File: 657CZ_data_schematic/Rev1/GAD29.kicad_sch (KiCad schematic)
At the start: 2 parts, among them J291 DE9_Socket, J292 DB25_Socket

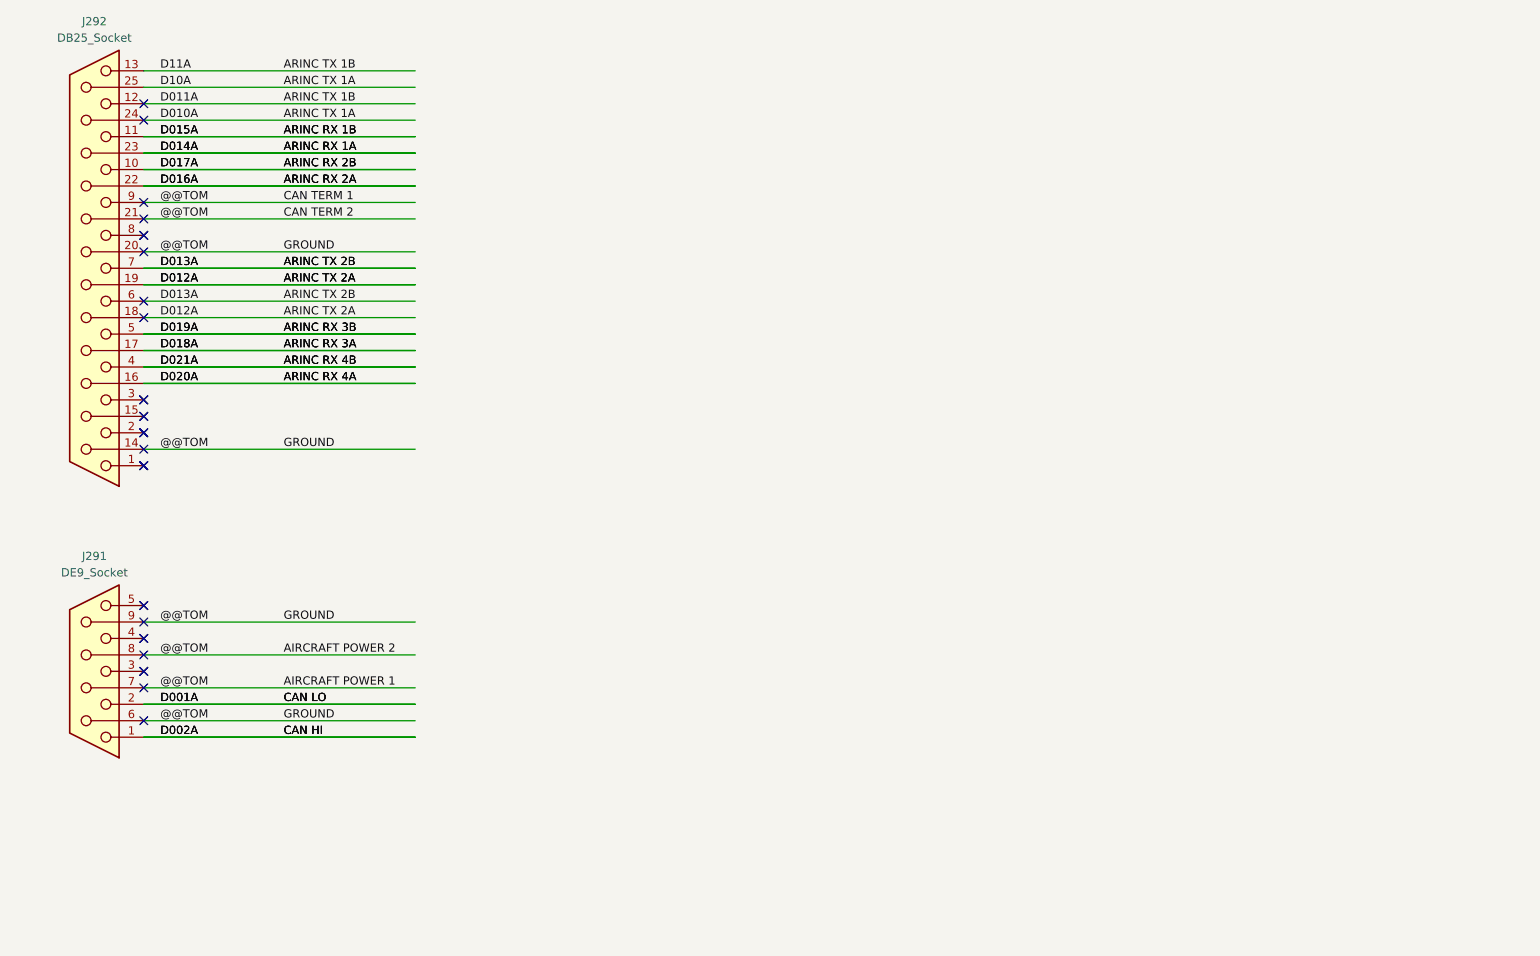
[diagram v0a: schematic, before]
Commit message: added data connections after AvClassics wiring. completed LRUs GMU, GDU, GSU, GAD, GNC, GTX, GTR  Not completed GMA, GEA and autopilot LRUs
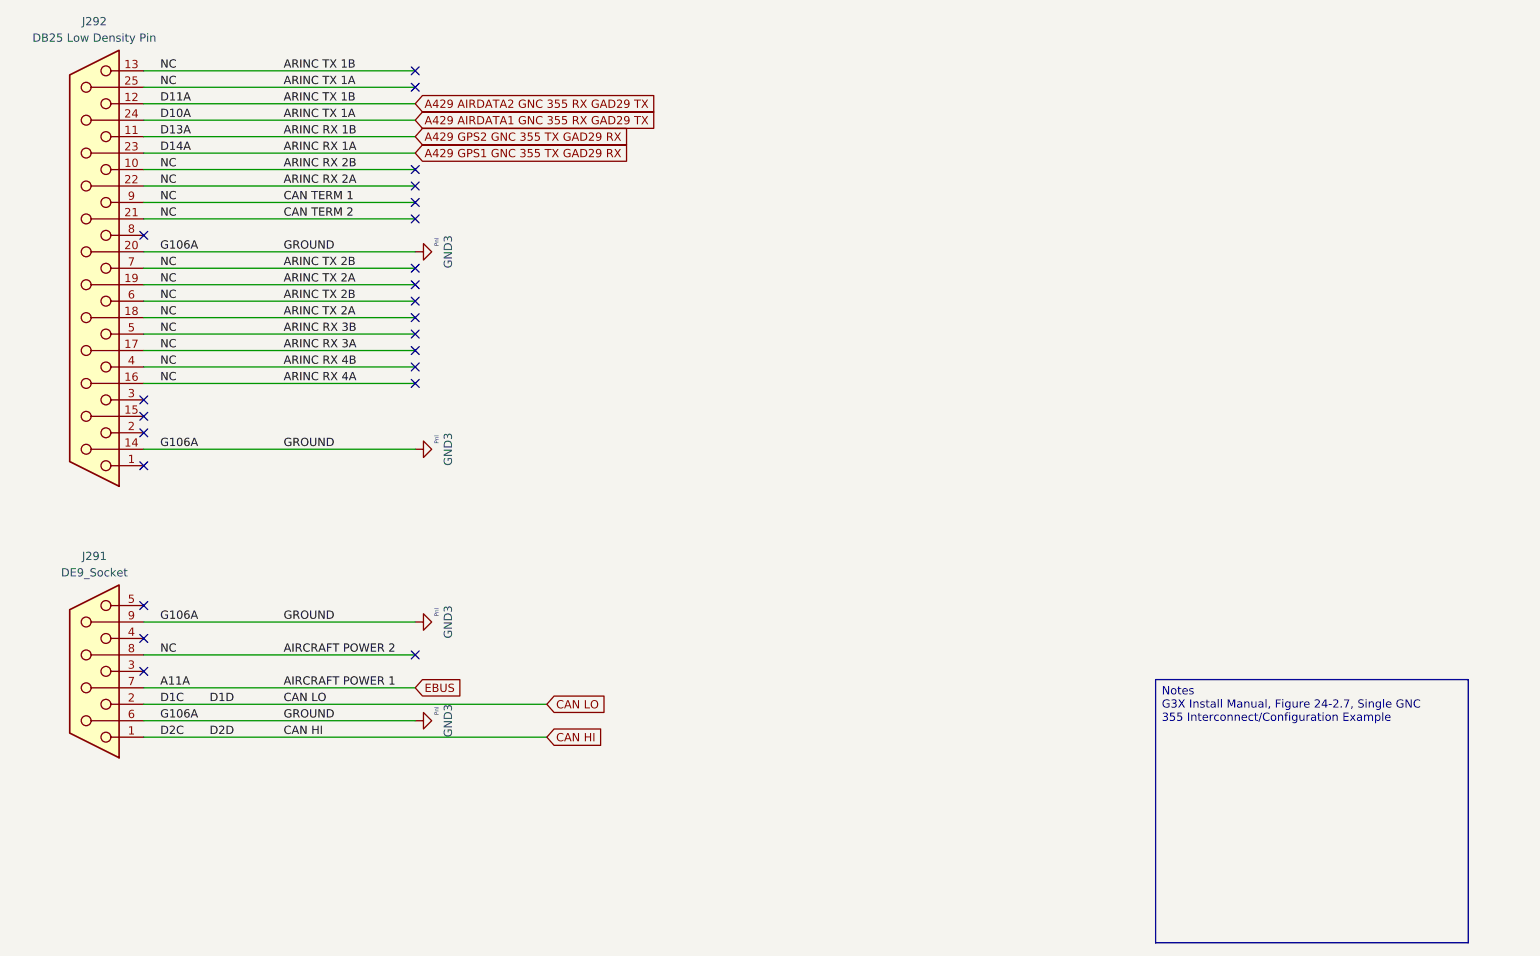
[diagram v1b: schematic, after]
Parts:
- J292: value DB25_Socket -> DB25 Low Density Pin
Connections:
- net ARINC RX 2B is gone; now on net A429 AIRDATA1 GNC 355 RX GAD29 TX: J292.10
- net ARINC RX 3A is gone; now on net A429 AIRDATA1 GNC 355 RX GAD29 TX: J292.17 (P17)
- net ARINC RX 3B is gone; now on net A429 AIRDATA1 GNC 355 RX GAD29 TX: J292.5
- net ARINC RX 4A is gone; now on net A429 AIRDATA1 GNC 355 RX GAD29 TX: J292.16 (P16)
- net ARINC RX 4B is gone; now on net A429 AIRDATA1 GNC 355 RX GAD29 TX: J292.4
- net ARINC TX 1A is gone; now on net A429 AIRDATA1 GNC 355 RX GAD29 TX: J292.24 (P24), J292.25 (P25)
- net ARINC TX 1B is gone; now on net A429 AIRDATA1 GNC 355 RX GAD29 TX: J292.12, J292.13
- net ARINC TX 2A is gone; now on net A429 AIRDATA1 GNC 355 RX GAD29 TX: J292.18 (P18), J292.19 (P19)
- net ARINC TX 2B is gone; now on net A429 AIRDATA1 GNC 355 RX GAD29 TX: J292.6, J292.7
- net @@TOM renamed GND3
- net GND3: no longer J291.7, J291.8, J292.21 (P21), J292.9
- net ARINC RX 1A renamed A429 GPS1 GNC 355 TX GAD29 RX
- net ARINC RX 1B renamed A429 GPS2 GNC 355 TX GAD29 RX
- net ARINC RX 2A renamed A429 AIRDATA1 GNC 355 RX GAD29 TX
- net A429 AIRDATA1 GNC 355 RX GAD29 TX: now also J291.8, J292.21 (P21), J292.9
- new net EBUS: J291.7
- no-connect marks 28 -> 23
